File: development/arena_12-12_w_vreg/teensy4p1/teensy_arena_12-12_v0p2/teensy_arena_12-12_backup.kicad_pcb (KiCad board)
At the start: 4 copper layers, 226.6 x 226.6 mm, 123 parts, among them J1 Barrel_Jack, J2 Conn_01x04, J3 Conn_01x04, P1 CONN15, P10 CONN15, P11 CONN15, P12 CONN15, P2 CONN15, P3 CONN15, P4 CONN15, P5 CONN15, P6 CONN15, P7 CONN15, P8 CONN15, P9 CONN15, Q2 MOSFET_NCHAN, SW1 SW_SPDT, U1 TXB0108PW, U10 TPS564201DDC, U11 TPS564201DDC, U12 TPS564201DDC, U13 TPS564201DDC, U14 TPS564201DDC, U15 TPS564201DDC, U16 TPS564201DDC, U17 TPS564201DDC, U18 Teensy4.1, U2 TXB0108PW, U3 TXB0108PW, U4 TXB0108PW, U5 TXB0108PW, U6 TPS564201DDC, U7 TPS564201DDC, U8 TPS564201DDC, U9 TPS564201DDC

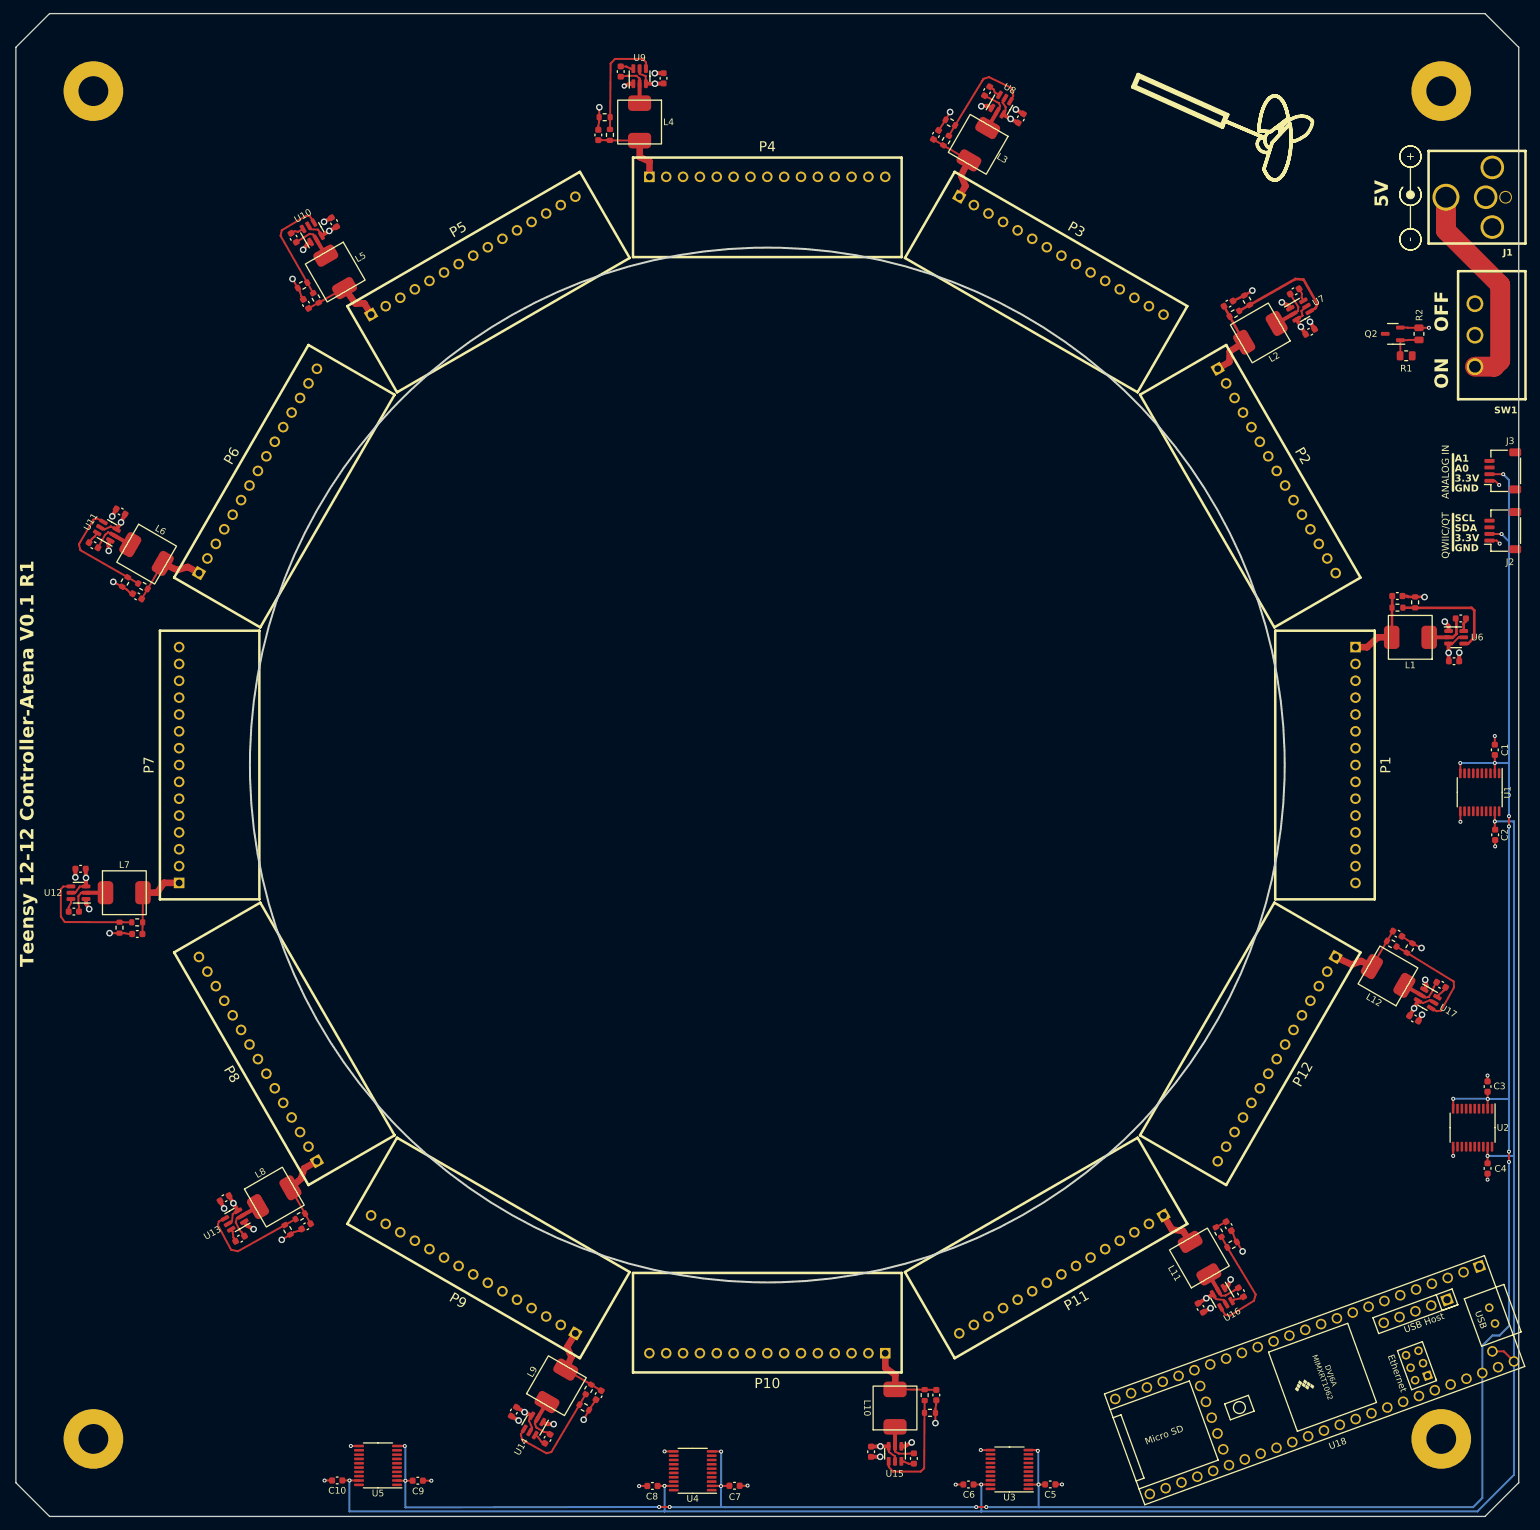
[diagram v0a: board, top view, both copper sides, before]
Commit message: Worked on routing for ni and teensy vreg arenas.
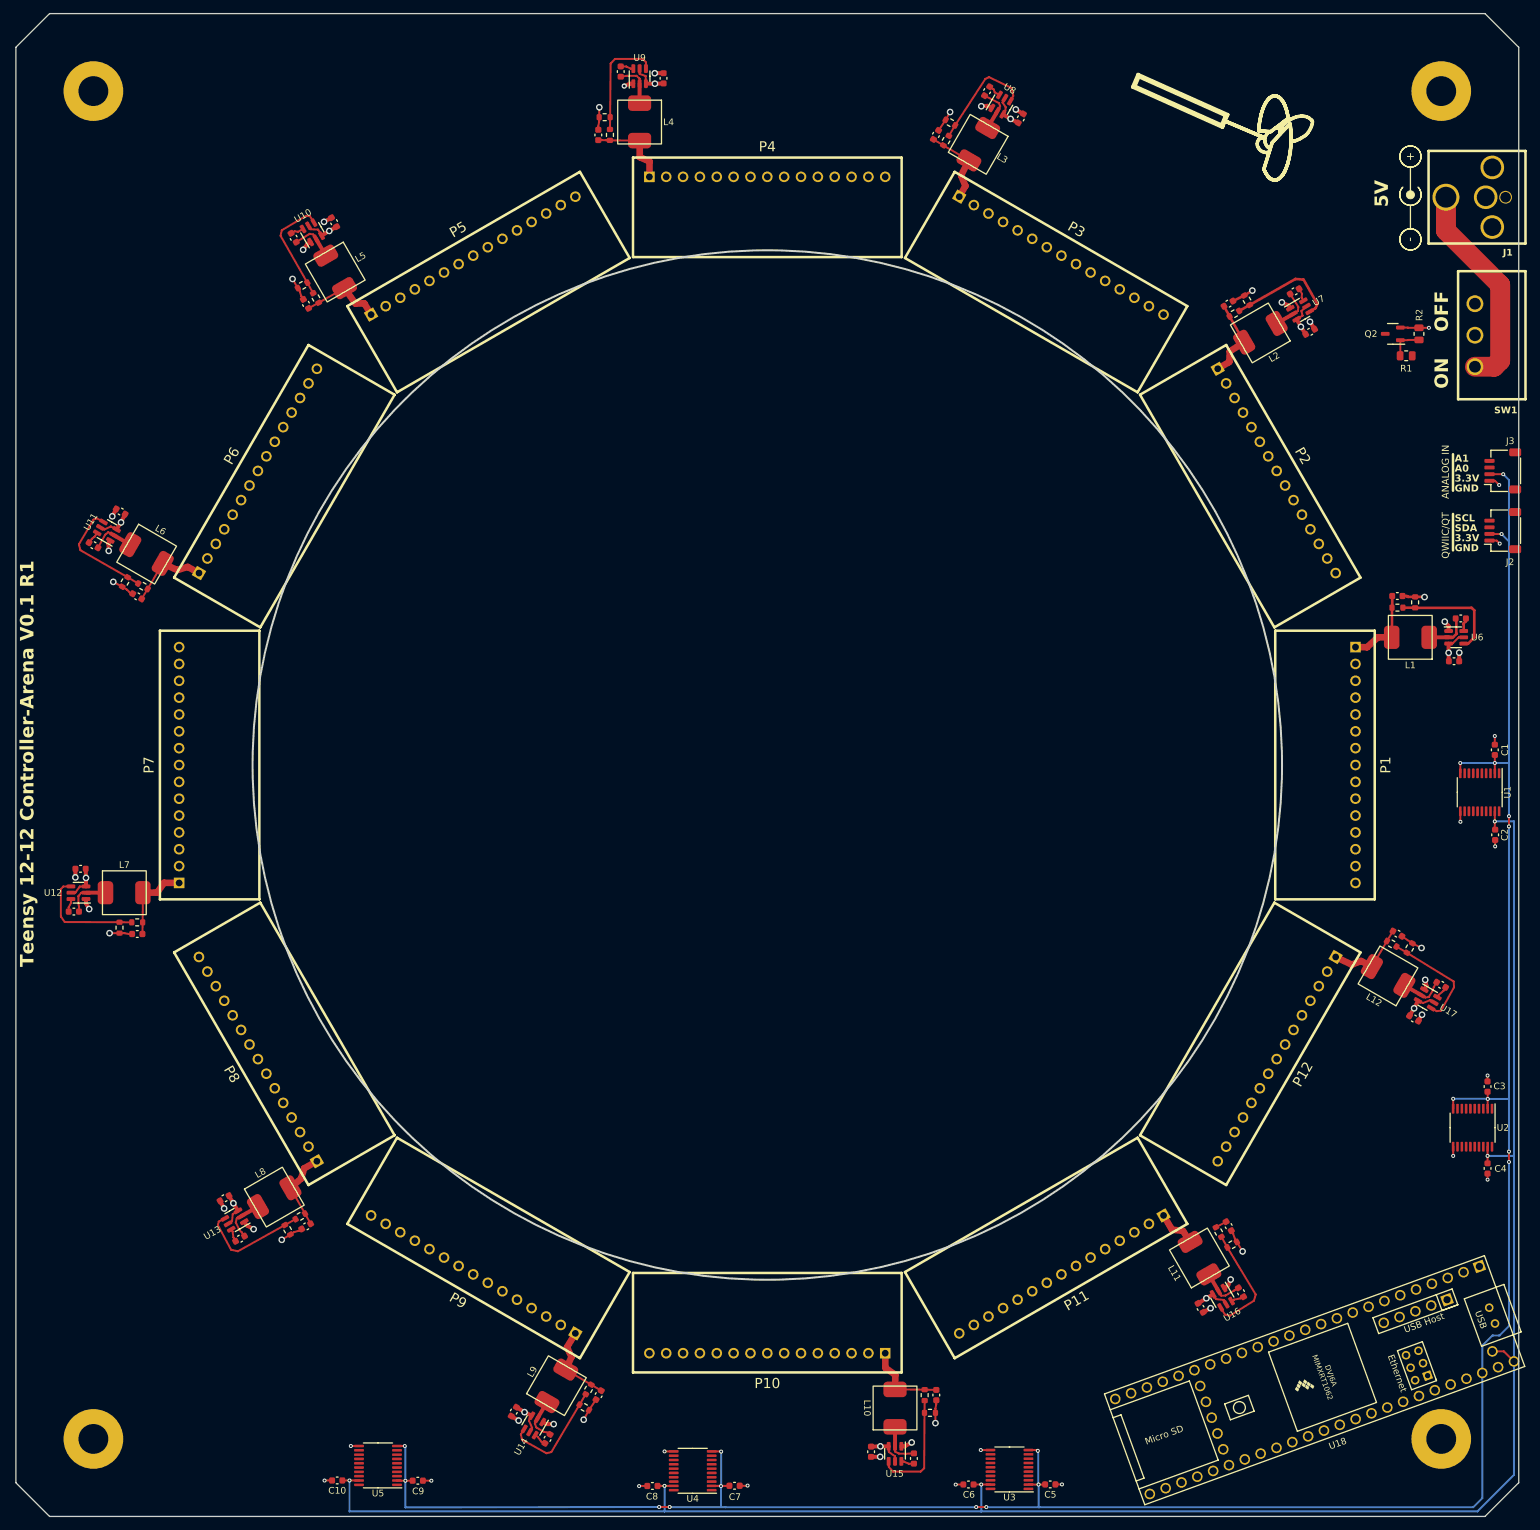
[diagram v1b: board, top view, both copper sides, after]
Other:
- outline, holes or cut-outs redrawn
